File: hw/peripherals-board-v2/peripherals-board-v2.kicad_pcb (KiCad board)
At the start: 2 copper layers, 75 x 55 mm, 18 parts

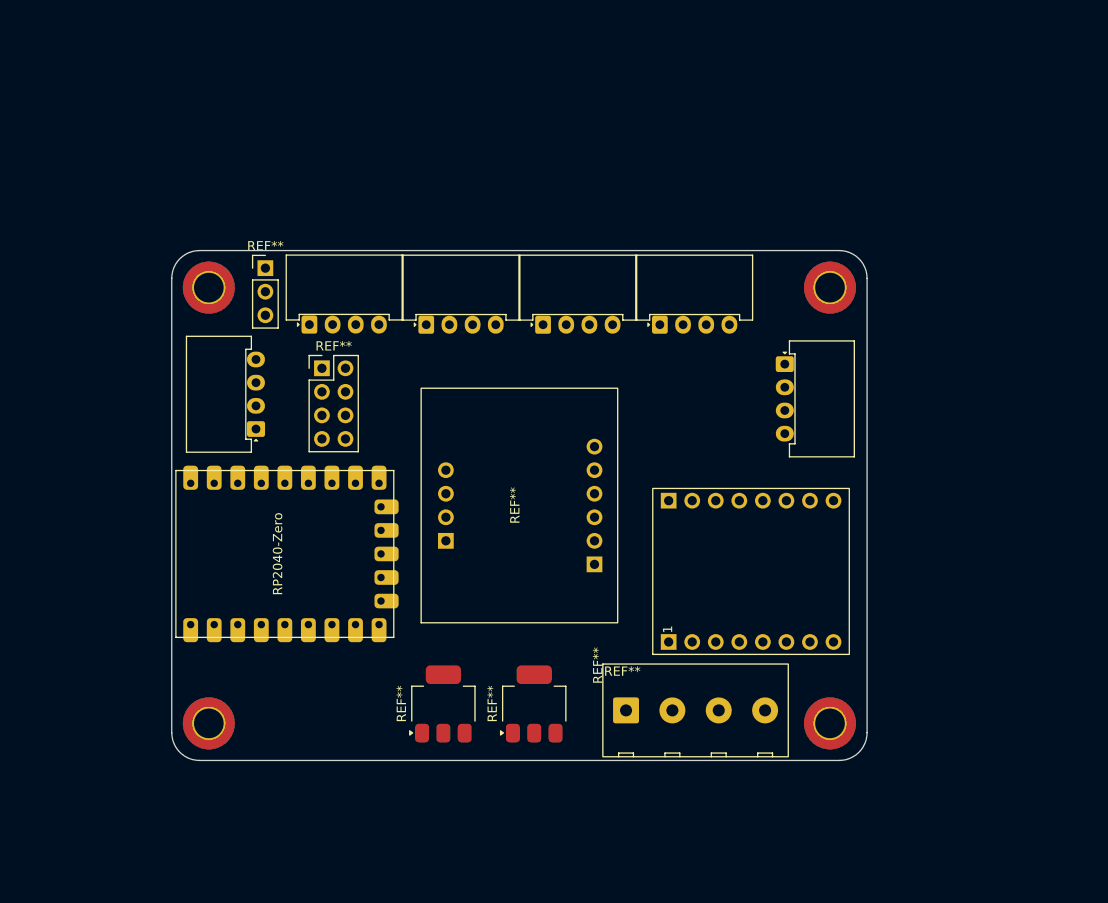
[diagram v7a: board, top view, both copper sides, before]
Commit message: Update peripherals board schematic and layout
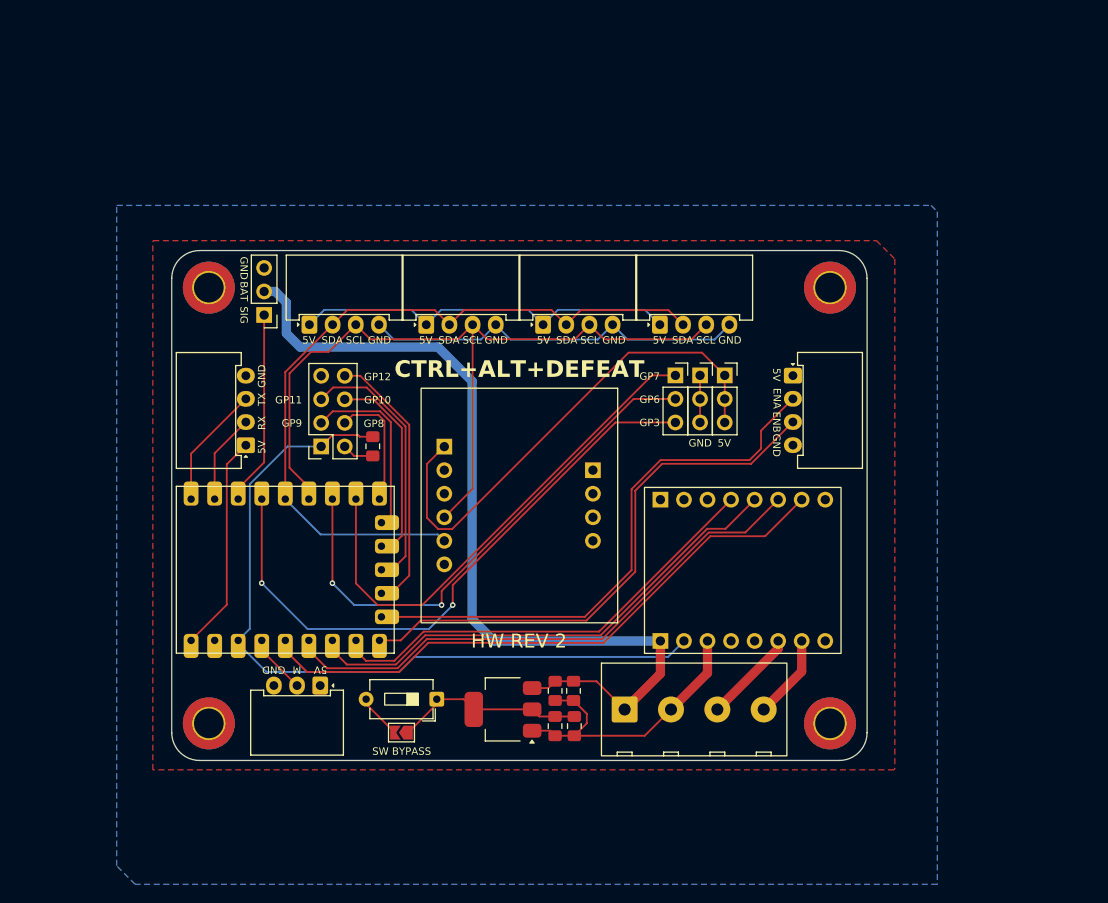
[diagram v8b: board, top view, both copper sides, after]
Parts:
- removed the REF** at (105.1, 59.2)
- removed the REF** at (66.5, 55.0)
- removed the REF** at (63.9, 89.9)
- removed the REF** at (53.9, 55.0)
- removed the REF** at (78.1, 95.9)
- removed the REF** at (79.0, 55.0)
- removed the REF** at (76.5, 74.5)
- removed the REF** at (48.1, 66.2)
- removed the REF** at (49.1, 48.9)
- removed the REF** at (92.6, 94.3)
- removed the REF** at (68.3, 95.9)
- removed the REF** at (91.7, 55.0)
- removed the REF** at (55.2, 59.7)
- removed the REF** at (92.8, 106.0)
- added C1: 0.1uF, Capacitor_SMD:C_0805_2012Metric_Pad1.18x1.45mm_HandSolder, F.Cu at (80.4, 94.5)
- added C2: 0.1uF, Capacitor_SMD:C_0805_2012Metric_Pad1.18x1.45mm_HandSolder, F.Cu at (80.3, 98.3)
- added C3: 10uF, Capacitor_SMD:C_0805_2012Metric_Pad1.18x1.45mm_HandSolder, F.Cu at (82.3, 94.5)
- added C4: 10uF, Capacitor_SMD:C_0805_2012Metric_Pad1.18x1.45mm_HandSolder, F.Cu at (82.4, 98.3)
- added C5: 10uF, Capacitor_SMD:C_0805_2012Metric_Pad1.18x1.45mm_HandSolder, F.Cu at (60.7, 68.1)
- added J1: Screw_Terminal_01x04, ScrewTerminal_01x04_P5mm:ScrewTerminal_01x04_P5mm, F.Cu at (92.7, 105.9)
- added J10: RF24, Connector_PinSocket_2.54mm:PinSocket_2x04_P2.54mm_Vertical, F.Cu at (55.1, 68.1)
- added J11: Conn_01x03, Connector_PinSocket_2.54mm:PinSocket_1x03_P2.54mm_Vertical, F.Cu at (93.3, 60.5)
- added J12: Conn_01x03, Connector_PinSocket_2.54mm:PinSocket_1x03_P2.54mm_Vertical, F.Cu at (96.0, 60.5)
- added J13: Conn_01x03, Connector_PinSocket_2.54mm:PinSocket_1x03_P2.54mm_Vertical, F.Cu at (98.6, 60.5)
- added J2: Conn_01x04_Socket, JST_XH_01x04_Horizontal_NoFlange:JST_XH_01x04_Horizontal_NoFlange, F.Cu at (79.0, 55.0)
- added J3: Conn_01x04_Socket, JST_XH_01x04_Horizontal_NoFlange:JST_XH_01x04_Horizontal_NoFlange, F.Cu at (91.7, 55.0)
- added J4: Conn_01x04_Socket, JST_XH_01x04_Horizontal_NoFlange:JST_XH_01x04_Horizontal_NoFlange, F.Cu at (53.9, 55.0)
- added J5: Conn_01x04_Socket, JST_XH_01x04_Horizontal_NoFlange:JST_XH_01x04_Horizontal_NoFlange, F.Cu at (66.5, 55.0)
- added J6: Conn_01x04_Socket, JST_XH_01x04_Horizontal_NoFlange:JST_XH_01x04_Horizontal_NoFlange, F.Cu at (106.0, 60.5)
- added J7: Conn_01x04_Socket, JST_XH_01x04_Horizontal_NoFlange:JST_XH_01x04_Horizontal_NoFlange, F.Cu at (47.0, 68.0)
- added J8: Conn_01x03_Socket, JST_XH_01x03_Horizontal_NoFlange:JST_XH_01x03_Horizontal_NoFlange, F.Cu at (52.2, 97.3)
- added J9: SERVO, Connector_PinHeader_2.54mm:PinHeader_1x03_P2.54mm_Vertical, F.Cu at (49.0, 54.0)
- added JP1: SolderJumper_2_Open, Jumper:SolderJumper-2_P1.3mm_Open_TrianglePad1.0x1.5mm, F.Cu at (63.8, 99.0)
- added RZ1: RP2040-Zero, RP2040-Zero:RP2040-Zero, F.Cu at (63.9, 91.6)
- added SW1: SW_DIP_x01, Button_Switch_THT:SW_DIP_SPSTx01_Slide_6.7x4.1mm_W7.62mm_P2.54mm_LowProfile, F.Cu at (67.6, 95.4)
- added U1: AMS1117-5.0, Package_TO_SOT_SMD:SOT-223-3_TabPin2, F.Cu at (74.7, 96.5)
- added U3: ~, TB6612FNG-breakout:TB6612FNG-breakout, F.Cu at (91.7, 94.2)
- added U4: ~, BNO055-breakout:BNO055-breakout, F.Cu at (76.5, 74.5)
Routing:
- net +5V: track 0.00 -> 125.9 mm
- net VBAT: track 0.00 -> 95.9 mm
- net /I2C0_SCL: track 0.00 -> 87.5 mm
- net +3.3V: track 0.00 -> 84.0 mm
- net GND: track 0.00 -> 82.6 mm
- net /I2C0_SDA: track 0.00 -> 81.7 mm
- net /GP3: track 0.00 -> 66.2 mm, vias 0 -> 2
- net /PWMB: track 0.00 -> 65.4 mm
- net /ENCA: track 0.00 -> 60.4 mm
- net /BIN2: track 0.00 -> 60.0 mm
- net /ENCB: track 0.00 -> 59.5 mm
- net /GP6: track 0.00 -> 57.1 mm, vias 0 -> 2
- net /GP7: track 0.00 -> 54.8 mm
- net /BIN1: track 0.00 -> 54.6 mm
- net /STBY: track 0.00 -> 49.2 mm
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- added copper zone on F.Cu, net +5V
- added copper zone on B.Cu, net GND
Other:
- board text added: "5V"
- board text added: "BAT"
- board text added: "CTRL+ALT+DEFEAT"
- board text added: "Designed by Adbhut Patil diylabsed.github.io/wro-25"
- board text added: "ENA"
- board text added: "ENB"
- board text added: "GND"
- board text added: "GP10"
- board text added: "GP11"
- board text added: "GP12"
- board text added: "GP3"
- board text added: "GP6"
- board text added: "GP7"
- board text added: "GP8"
- board text added: "GP9"
- board text added: "HW REV 2"
- board text added: "M"
- board text added: "Peripherals Board HW Revision 2"
- board text added: "RX"
- board text added: "SCL"
- board text added: "SDA"
- board text added: "SIG"
- board text added: "SW BYPASS"
- board text added: "TX"
